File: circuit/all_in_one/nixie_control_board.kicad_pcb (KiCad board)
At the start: 2 copper layers, 131.4 x 42.3 mm, 68 parts, among them CON1 BARREL_JACK, IC1 ATMEGA328P-A, P1 CONN_01X08, P2 CONN_02X03, P3 CONN_01X12, P4 CONN_02X04, P5 CONN_01X08, P6 CONN_01X12, Q1 2SB647, Q2 2SK2611, Q3 Q_NPN_EBC, Q4 Q_NPN_EBC, SW1 SW_PUSH, U1 SMD_7805, U10 IN-14, U11 IN-14, U12 IN-14, U13 IN-14, U14 IN-14, U15 IN-14, U16 IN-14, U17 IN-14, U18 DFPlayer, U2 MC34063A, U3 TLP521, U4 TLP521, U5 HEF4028, U6 TLP521, U7 TLP521, U8 K155ID1, U9 DS1307, Y1 16MHZ, Y2 32.768khz

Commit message: Finish the layout of power supply part
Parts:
- moved C5 9.22 mm to (58.9, 155.9), turned to 90 degrees
- moved R12 4.30 mm to (85.9, 158.6)
- moved R15 4.30 mm to (77.6, 158.6)
- moved R16 4.30 mm to (82.7, 158.6)
- moved R10 4.30 mm to (80.2, 158.6)
- moved P4 3.58 mm to (99.3, 150.2)
- moved R4 3.33 mm to (41.2, 163.9), turned to 180 degrees
- moved P2 3.28 mm to (96.6, 161.3), turned to 90 degrees
- moved C2 3.15 mm to (27.4, 165.8), turned to 90 degrees
- moved U1 3.14 mm to (52.8, 158.3)
- moved R5 1.45 mm to (41.2, 166.4), turned to 180 degrees
- moved C1 1.06 mm to (40.8, 154.7)
- turned R11 to 270 degrees
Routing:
- net /RTC/GND: track 0.00 -> 234.5 mm
- net /power_supply/12V: track 0.00 -> 82.0 mm
- net Net-(R8-Pad2): track 0.00 -> 59.4 mm
- net Net-(R9-Pad1): track 0.00 -> 56.2 mm
- net Net-(R6-Pad2): track 0.00 -> 46.0 mm
- net Net-(L1-Pad1): track 0.00 -> 44.6 mm
- net Net-(D1-Pad2): track 0.00 -> 42.0 mm
- net Net-(C6-Pad1): track 0.00 -> 33.5 mm
- net Net-(R4-Pad2): track 0.00 -> 28.6 mm
- net Net-(D2-Pad2): track 0.00 -> 21.1 mm
- net Net-(R5-Pad2): track 0.00 -> 20.0 mm
- net /RTC/5V: track 0.00 -> 13.3 mm
- net /nixie_control/170V: track 0.00 -> 12.6 mm
- net Net-(D1-Pad1): track 0.00 -> 11.5 mm
- net Reset: track 0.00 -> 7.95 mm
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
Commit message: More works on PCB layout...
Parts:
- BT1: footprint Connect:CR2032H -> cr1220_smd:cr1220smd; moved to F.Cu
- U18: moved to B.Cu
- moved R8 94.6 mm to (136.9, 136.8), turned to 270 degrees
- moved R16 92.4 mm to (168.1, 123.2), turned to 0 degrees
- moved R11 81.2 mm to (132.8, 136.7)
- moved R19 62.3 mm to (168.0, 118.3), turned to 0 degrees
- moved R15 59.9 mm to (120.1, 116.4), turned to 90 degrees
- moved R10 58.9 mm to (134.8, 136.7)
- moved R14 57.4 mm to (148.9, 128.2)
- moved R18 57.2 mm to (168.0, 120.7), turned to 0 degrees
- moved P2 54.9 mm to (119.3, 111.2)
- moved P4 53.6 mm to (133.0, 108.6)
- moved Y1 52.7 mm to (156.3, 118.5)
- moved R12 52.6 mm to (105.9, 110.0), turned to 0 degrees
- moved C8 51.2 mm to (159.2, 114.6), turned to 180 degrees
- moved U5 50.8 mm to (156.8, 128.1)
- moved C9 50.1 mm to (153.5, 114.5), turned to 0 degrees
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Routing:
- net /RTC/GND: track 234.5 -> 454.6 mm, vias 0 -> 9
- net /RTC/5V: track 13.3 -> 188.7 mm, vias 0 -> 4
- net Net-(P1-Pad3): track 0.00 -> 68.9 mm, vias 0 -> 2
- net Net-(R9-Pad1): track 56.2 -> 124.6 mm, vias 0 -> 2
- net Net-(P1-Pad4): track 0.00 -> 67.7 mm, vias 0 -> 2
- net /RTC/I2C_SCL: track 0.00 -> 57.9 mm, vias 0 -> 4
- net Font_C: track 0.00 -> 54.4 mm, vias 0 -> 1
- net Net-(P1-Pad5): track 0.00 -> 52.0 mm
- net /RTC/I2C_SDA: track 0.00 -> 51.0 mm, vias 0 -> 2
- net Net-(P1-Pad2): track 0.00 -> 50.5 mm, vias 0 -> 2
- net Net-(P1-Pad1): track 0.00 -> 50.1 mm, vias 0 -> 2
- net Net-(P1-Pad6): track 0.00 -> 49.0 mm
- net Font_B: track 0.00 -> 47.6 mm, vias 0 -> 1
- net MP3_TX: track 0.00 -> 47.3 mm, vias 0 -> 2
- net Net-(P1-Pad7): track 0.00 -> 46.0 mm
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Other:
- board size 131.4 x 42.3 mm -> 136.5 x 42.3 mm

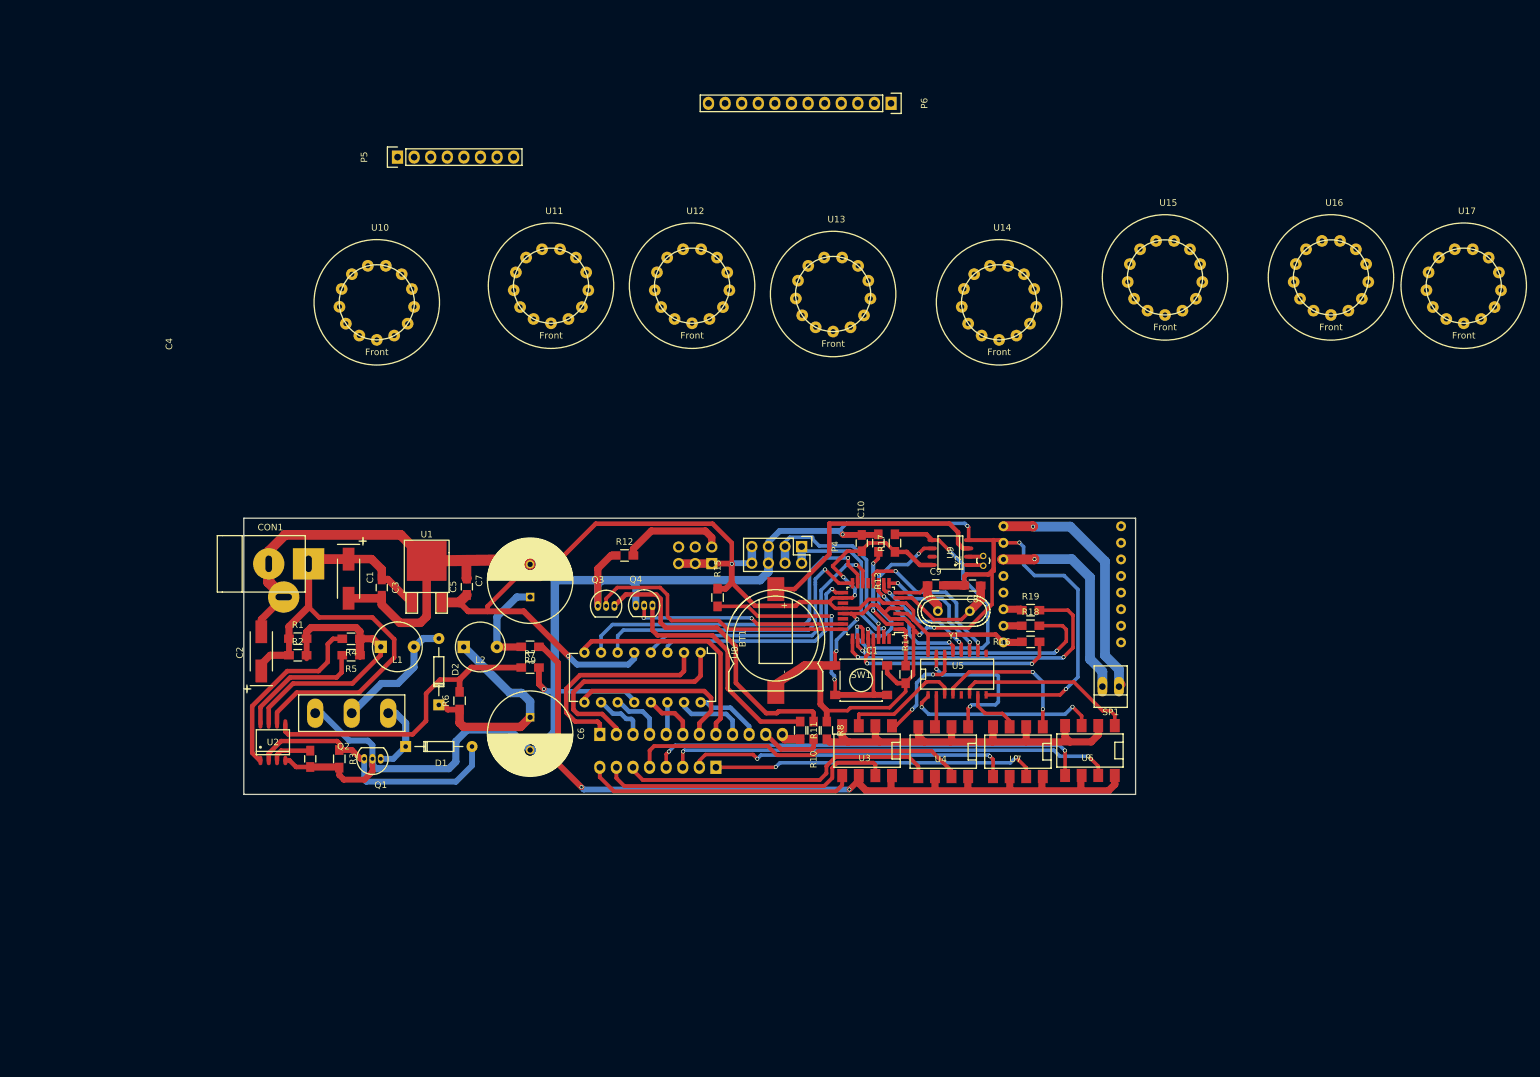
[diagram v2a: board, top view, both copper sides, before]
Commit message: New hardware is almost finished
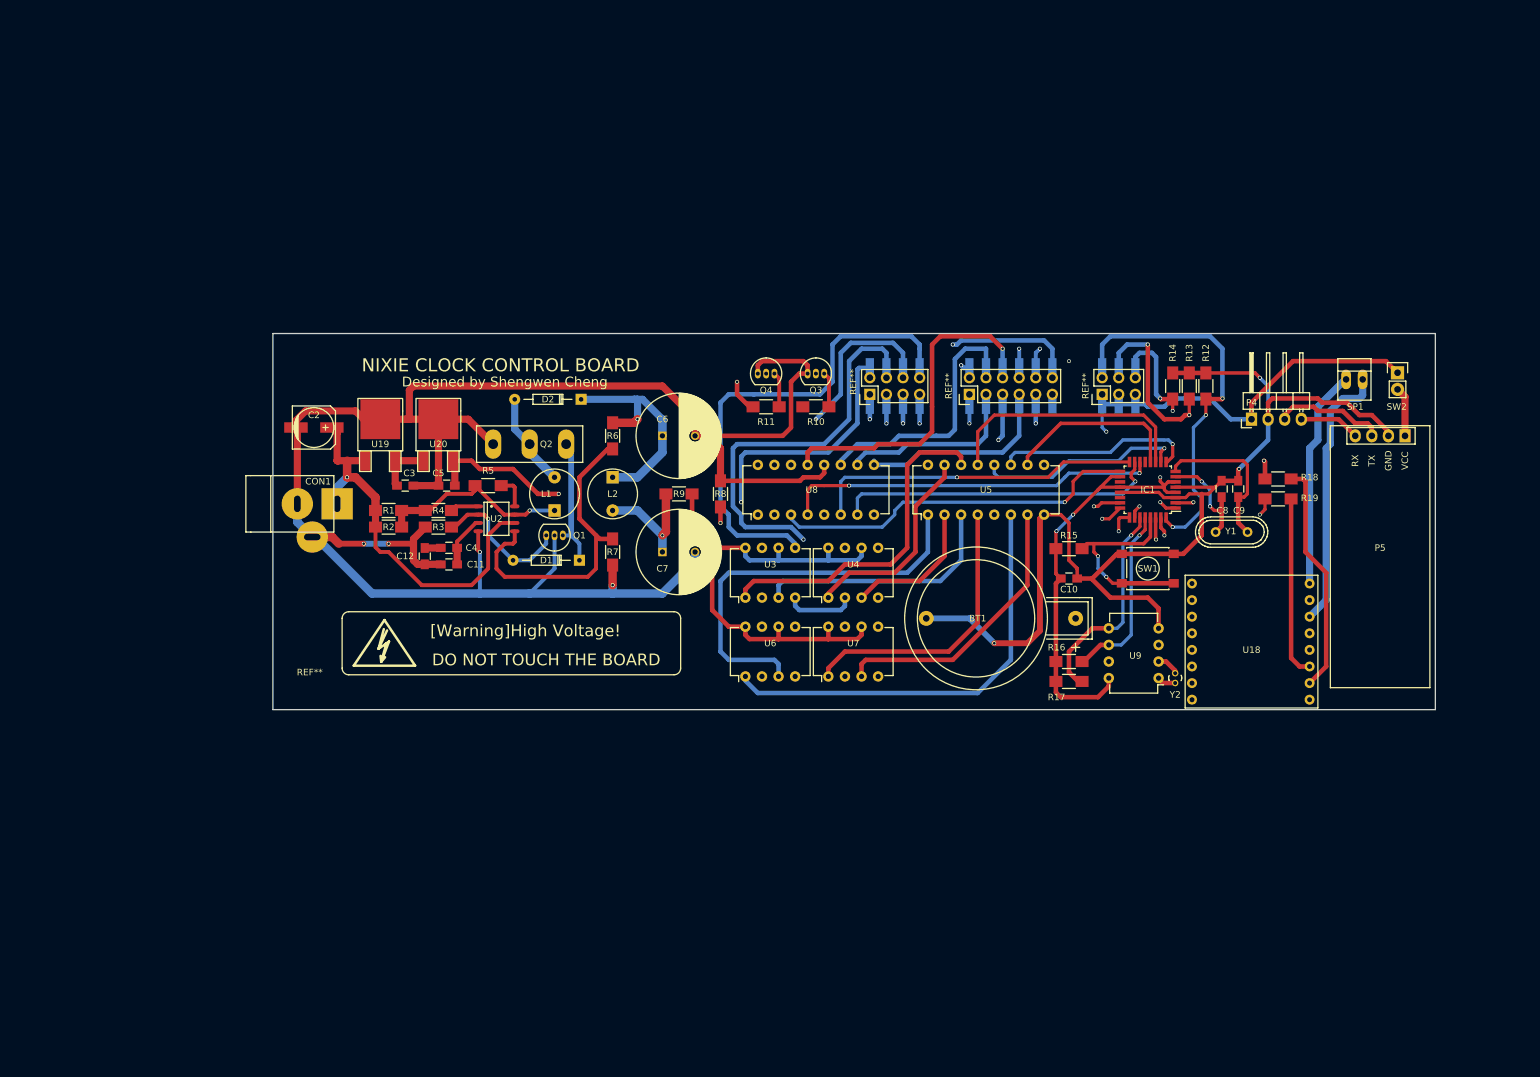
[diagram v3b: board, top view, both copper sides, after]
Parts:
- removed C1: 100uf, Capacitors_Tantalum_SMD:TantalC_SizeC_EIA-6032_HandSoldering
- removed P6: CONN_01X12, Pin_Headers:Pin_Header_Straight_1x12
- removed U1: SMD_7805, TO_SOT_Packages_SMD:TO-252-2Lead
- removed U10, U11, U12, U13, U14, U15, U16, U17: IN-14, IN-14:IN-14
- added C11: 1000pf, Capacitors_SMD:C_0805_HandSoldering, F.Cu at (79.0, 111.3)
- added C12: 1000pf, Capacitors_SMD:C_0805_HandSoldering, F.Cu at (75.3, 110.1)
- added REF**: Symbol_HighVoltage_Type2_CopperTop_VerySmall, warning:warning, F.Cu at (69.1, 124.0)
- added REF**: Pin_Header_Straight_2x04, Pin_Headers:Pin_Header_Straight_2x04, F.Cu at (143.4, 85.3)
- added REF**: Pin_Header_Straight_2x06, Pin_Headers:Pin_Header_Straight_2x06, F.Cu at (158.7, 85.3)
- added REF**: Pin_Header_Straight_2x03, Pin_Headers:Pin_Header_Straight_2x03, F.Cu at (179.0, 85.3)
- added SW2: SPST, Pin_Headers:Pin_Header_Straight_1x02, F.Cu at (224.2, 82.0)
- added U19: LM7808CT, TO_SOT_Packages_SMD:TO-252-2Lead, F.Cu at (68.5, 95.5)
- added U20: SMD_7805, TO_SOT_Packages_SMD:TO-252-2Lead, F.Cu at (77.4, 95.5)
- BT1: footprint cr1220_smd:cr1220smd -> Connect:CR2032H
- C2: footprint Capacitors_Tantalum_SMD:TantalC_SizeC_EIA-6032_HandSoldering -> Capacitors_SMD:c_elec_6.3x5.3
- C4: value 1500pf -> 1000pf
- P1: footprint Pin_Headers:Pin_Header_Straight_1x08 -> SMD_PIN_2_BY_4_REVERSE:SMD_PIN_2_BY_4_REVERSE
- P2: footprint Pin_Headers:Pin_Header_Straight_2x03 -> SMD_PIN_2_BY_3_REVERSE:SMD_PIN_2_BY_3_REVERSE
- P3: footprint Pin_Headers:Pin_Header_Straight_1x12 -> SMD_PIN_2_BY_6_REVERSE:SMD_PIN_2_BY_6_REVERSE
- P4: value CONN_02X04 -> CONN_01X04; footprint Pin_Headers:Pin_Header_Straight_2x04 -> Pin_Headers:Pin_Header_Angled_1x04
- P5: value CONN_01X08 -> BLUETOOTH_SJ; footprint Pin_Headers:Pin_Header_Straight_1x08 -> HC06:HC06
- R1, R10, R11, R12, R13, R14, R15, R16, R17, R18, R19, R2, R3, R4, R5, R6, R7, R8, R9: footprint Resistors_SMD:R_0805_HandSoldering -> Resistors_SMD:R_1206_HandSoldering
- U18: moved to F.Cu
- U3, U4, U6, U7: footprint SMD_Packages:DIP-8_SMD -> Housings_DIP:DIP-8_W7.62mm
- U5: footprint SMD_Packages:SO-16-N -> Housings_DIP:DIP-16_W7.62mm
- U9: footprint Power_Integrations:SO-8 -> Housings_DIP:DIP-8_W7.62mm
- moved P5 160.0 mm to (225.4, 91.7), turned to 270 degrees
- moved R12 92.7 mm to (194.9, 84.0), turned to 270 degrees
- moved P3 76.9 mm to (158.7, 85.3), turned to 0 degrees
- moved P4 71.6 mm to (201.9, 89.1), turned to 90 degrees
- moved P2 65.1 mm to (179.0, 85.3), turned to 0 degrees
- moved P1 61.8 mm to (143.4, 85.3), turned to 0 degrees
- moved R14 60.1 mm to (189.8, 84.0), turned to 270 degrees
- moved SP1 60.0 mm to (217.6, 83.0), turned to 0 degrees
- moved R15 54.3 mm to (173.9, 108.9), turned to 180 degrees
- moved U6 53.9 mm to (124.4, 128.5), turned to 90 degrees
- moved R13 53.3 mm to (192.3, 84.0)
- moved D2 51.6 mm to (99.2, 86.1), turned to 180 degrees
- moved R11 49.8 mm to (127.6, 87.2), turned to 180 degrees
- moved R10 49.5 mm to (135.2, 87.2), turned to 180 degrees
- moved Q2 49.4 mm to (91.4, 92.9)
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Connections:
- C3 pad 1: /power_supply/12V -> Net-(C3-Pad1)
- C4 pad 2: /RTC/GND -> Net-(C12-Pad1)
- P4 pad 1: USART_TX -> /RTC/5V
- P4 pad 2: USART_TX -> /RTC/GND
- P4 pad 4: USART_RX -> USART_TX
- P5 pad 1: anode8 -> USART_TX
- P5 pad 2: anode7 -> USART_RX
- P5 pad 3: anode6 -> /RTC/GND
- P5 pad 4: anode5 -> Net-(P5-Pad4)
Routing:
- net /RTC/GND: track 454.6 -> 570.2 mm, vias 9 -> 8
- net /RTC/5V: track 188.7 -> 265.3 mm, vias 4 -> 5
- net Net-(P3-Pad10): track 10.2 -> 80.6 mm, vias 0 -> 1
- net _cathode_comma_right: track 3.28 -> 62.8 mm, vias 0 -> 2
- net right_comma: track 32.8 -> 82.8 mm, vias 2 -> 1
- net Net-(R9-Pad1): track 124.6 -> 80.1 mm, vias 2 -> 0
- net Mode_button: track 16.0 -> 59.3 mm, vias 0 -> 3
- net Net-(P3-Pad6): track 8.11 -> 50.7 mm, vias 0 -> 1
- net USART_RX: track 30.5 -> 71.9 mm
- net Net-(Q3-Pad3): track 45.7 -> 5.38 mm
- net Net-(BT1-Pad1): track 39.0 -> 0.00 mm
- net Net-(U5-Pad6): track 27.4 -> 66.4 mm
- net Net-(P3-Pad5): track 4.99 -> 42.5 mm, vias 0 -> 1
- net Net-(U3-Pad1): track 16.3 -> 51.9 mm, vias 2 -> 0
- net Net-(P3-Pad9): track 11.5 -> 47.1 mm, vias 0 -> 1
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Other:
- board size 136.5 x 42.3 mm -> 177.9 x 57.6 mm
- copper layers 2 -> 4
- board text added: "DO NOT TOUCH THE BOARD"
- board text added: "Designed by Shengwen Cheng"
- board text added: "NIXIE CLOCK CONTROL BOARD"
- board text added: "[Warning]High Voltage!"

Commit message: Create footprint common library
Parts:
- removed REF**: Symbol_HighVoltage_Type2_CopperTop_VerySmall, warning:warning
- removed REF**: Pin_Header_Straight_2x04, Pin_Headers:Pin_Header_Straight_2x04
- removed REF**: Pin_Header_Straight_2x06, Pin_Headers:Pin_Header_Straight_2x06
- removed REF**: Pin_Header_Straight_2x03, Pin_Headers:Pin_Header_Straight_2x03
